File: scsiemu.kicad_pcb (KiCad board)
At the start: 2 copper layers, 65 x 41.7 mm, 38 parts, among them J1 RasPi, J2 SCSI, J3 USB_POWER, J4 POWER 5V, J5 I2C, U1 74LS641-1, U2 74LS641-1, U3 74LS641-1, U4 74LS641-1

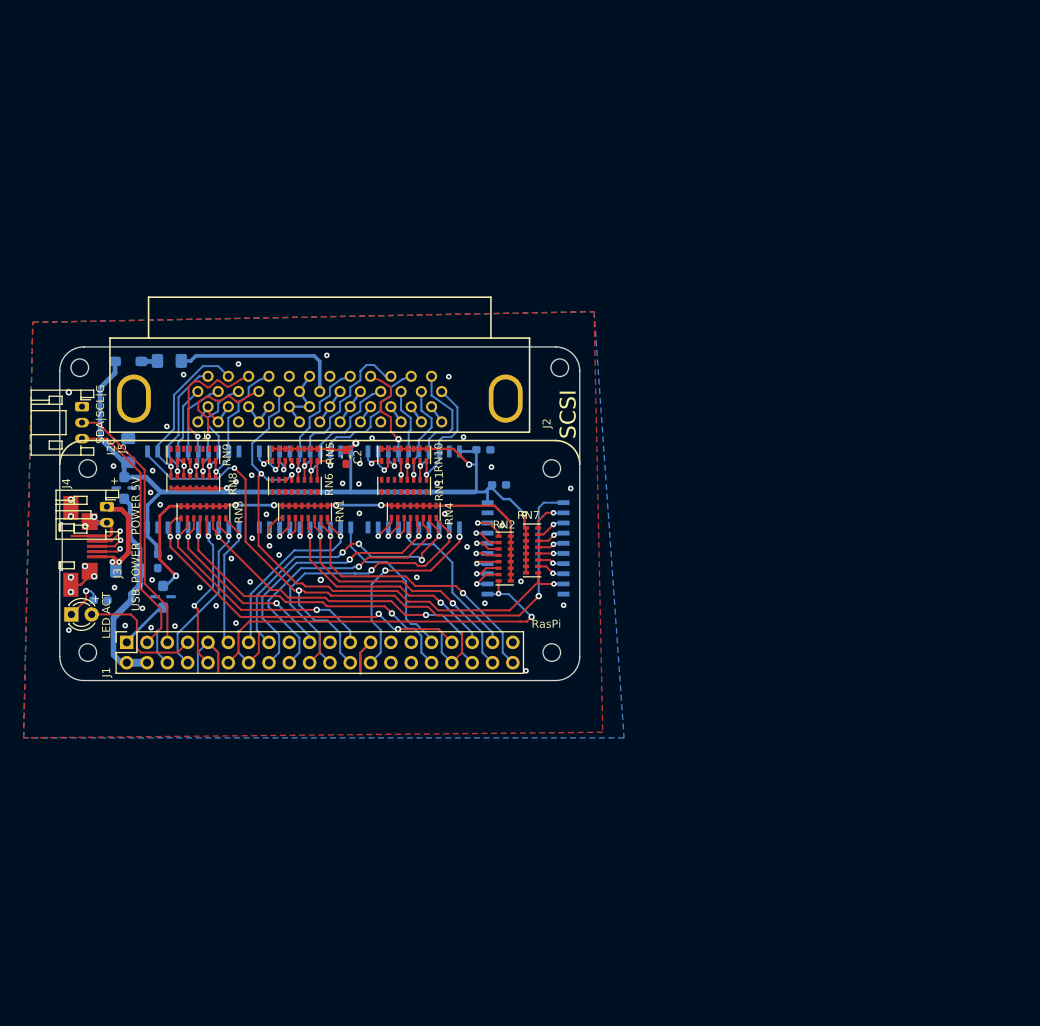
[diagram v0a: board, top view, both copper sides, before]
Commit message: Internal 50pin version (#1)
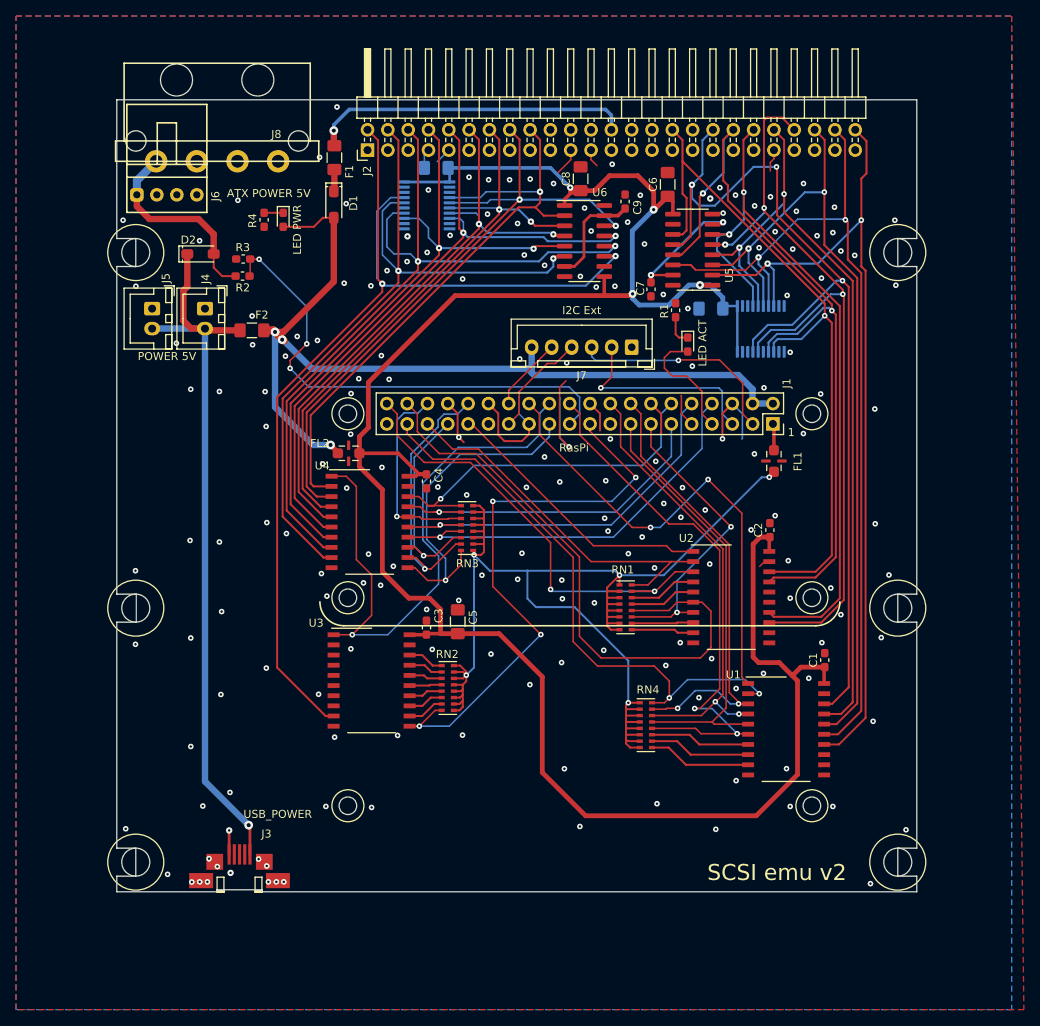
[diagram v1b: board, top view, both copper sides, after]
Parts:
- removed REF** (x6): MountingHole_2.2mm_M2, MountingHole:MountingHole_2.2mm_M2
- removed RN10, RN5, RN7, RN8: 220, Resistor_SMD:R_Cat16-8
- removed RN11, RN6, RN9: 330, Resistor_SMD:R_Cat16-8
- added C10: 10u, Capacitor_SMD:C_1206_3216Metric_Pad1.42x1.75mm_HandSolder, B.Cu at (183.9, 64.0)
- added C11: 10u, Capacitor_SMD:C_1206_3216Metric_Pad1.42x1.75mm_HandSolder, B.Cu at (149.6, 46.4)
- added C6: 10u, Capacitor_SMD:C_1206_3216Metric_Pad1.42x1.75mm_HandSolder, F.Cu at (178.5, 48.5)
- added C7: 2.2u, Capacitor_SMD:C_0603_1608Metric_Pad1.05x0.95mm_HandSolder, F.Cu at (176.4, 61.6)
- added C8: 10u, Capacitor_SMD:C_1206_3216Metric_Pad1.42x1.75mm_HandSolder, F.Cu at (167.6, 47.8)
- added C9: 2.2u, Capacitor_SMD:C_0603_1608Metric_Pad1.05x0.95mm_HandSolder, F.Cu at (173.2, 50.6)
- added D2: SBD, local_lib:D_SOD-123_HandSoldering, F.Cu at (120.1, 57.2)
- added J6: AT Power 5V (171826-4), local_lib:Molex_171826-4, F.Cu at (119.6, 49.8)
- added J7: I2C Ext, Connector_JST:JST_XH_B6B-XH-A_1x06_P2.50mm_Vertical, F.Cu at (174.0, 68.8)
- added J8: AT Power 5V (641737-1), local_lib:TE_641737-1, F.Cu at (122.2, 35.4)
- added LED2: LED ACT, LED_SMD:LED_0603_1608Metric_Pad1.05x0.95mm_HandSolder, F.Cu at (181.0, 68.5)
- added MH1: Raspi Mount, MountingHole:MountingHole_2.2mm_M2, F.Cu at (138.5, 100.2)
- added MH10: Raspi Mount, MountingHole:MountingHole_2.2mm_M2, F.Cu at (138.5, 126.2)
- added MH11: HDD Mount, MountingHole:MountingHole_3.5mm, F.Cu at (112.0, 101.5)
- added MH12: HDD Mount, MountingHole:MountingHole_3.5mm, F.Cu at (207.2, 101.5)
- added MH2: Raspi Mount, MountingHole:MountingHole_2.2mm_M2, F.Cu at (138.5, 77.2)
- added MH3: Raspi Mount, MountingHole:MountingHole_2.2mm_M2, F.Cu at (196.5, 77.2)
- added MH4: Raspi Mount, MountingHole:MountingHole_2.2mm_M2, F.Cu at (196.5, 100.2)
- added MH5: HDD Mount, MountingHole:MountingHole_3.5mm, F.Cu at (112.0, 57.0)
- added MH6: HDD Mount, MountingHole:MountingHole_3.5mm, F.Cu at (112.0, 133.2)
- added MH7: HDD Mount, MountingHole:MountingHole_3.5mm, F.Cu at (207.2, 57.0)
- added MH8: HDD Mount, MountingHole:MountingHole_3.5mm, F.Cu at (207.2, 133.2)
- added MH9: Raspi Mount, MountingHole:MountingHole_2.2mm_M2, F.Cu at (196.5, 126.2)
- added R2: 2.2k, Resistor_SMD:R_0603_1608Metric_Pad1.05x0.95mm_HandSolder, F.Cu at (125.3, 59.9)
- added R3: 2.7k, Resistor_SMD:R_0603_1608Metric_Pad1.05x0.95mm_HandSolder, F.Cu at (125.4, 57.8)
- added R4: 1k, Resistor_SMD:R_0603_1608Metric_Pad1.05x0.95mm_HandSolder, F.Cu at (128.0, 52.9)
- added U5: DS2105Z, Package_SO:SOIC-16_3.9x9.9mm_P1.27mm, F.Cu at (181.6, 56.6)
- added U6: DS2105Z, Package_SO:SOIC-16_3.9x9.9mm_P1.27mm, F.Cu at (168.1, 55.6)
- added U7: TL2218-285, Package_SO:TSSOP-20_4.4x6.5mm_P0.65mm, B.Cu at (190.1, 66.5)
- added U8: TL2218-285, Package_SO:TSSOP-20_4.4x6.5mm_P0.65mm, B.Cu at (148.4, 51.1)
- C1, C4: value 0.1u JB -> 0.1u; moved to F.Cu
- C2: value 0.1u JB -> 0.1u
- C3: value 0.1u JIS B -> 0.1u; moved to F.Cu
- C5: value 10u JB -> 10u; moved to F.Cu
- D1: footprint cd_device:D_SOD-123_HandSoldering -> local_lib:D_SOD-123_HandSoldering; moved to F.Cu
- F1: value 1A -> 750mA ~~ 1A (0ZCJ0075FF2E); moved to F.Cu
- F2: value 1A -> 2A (0685T2000-01); moved to F.Cu
- FL1, FL2, R1, U1, U2, U3, U4: moved to F.Cu
- J2: footprint local_lib:DSUB50P -> Connector_PinHeader_2.54mm:PinHeader_2x25_P2.54mm_Horizontal
- J4: footprint Connector_JST:JST_PH_S2B-PH-K_1x02_P2.00mm_Horizontal -> Connector_JST:JST_XH_B2B-XH-A_1x02_P2.50mm_Vertical
- J5: value I2C -> POWER 5V; footprint Connector_JST:JST_PH_S3B-PH-K_1x03_P2.00mm_Horizontal -> Connector_JST:JST_XH_B2B-XH-A_1x02_P2.50mm_Vertical
- LED1: value LED ACT -> LED PWR; footprint LED_THT:LED_D3.0mm -> LED_SMD:LED_0603_1608Metric_Pad1.05x0.95mm_HandSolder
- moved J1 85.3 mm to (191.6, 78.4), turned to 270 degrees
- moved R1 80.5 mm to (179.5, 64.2), turned to 90 degrees
- moved FL1 78.2 mm to (191.8, 83.1), turned to 270 degrees
- moved LED1 56.0 mm to (130.4, 52.9), turned to 270 degrees
- moved U1 55.4 mm to (193.3, 116.6), turned to 0 degrees
- moved U2 55.0 mm to (186.4, 100.1), turned to 0 degrees
- moved C2 53.7 mm to (191.3, 91.7), turned to 90 degrees
- moved C1 50.1 mm to (198.1, 108.0), turned to 90 degrees
- moved J3 46.8 mm to (125.0, 135.5), turned to 0 degrees
- moved C5 46.4 mm to (152.2, 103.1)
- moved RN1 41.8 mm to (173.2, 101.3), turned to 180 degrees
- moved RN4 39.4 mm to (175.8, 116.1), turned to 180 degrees
- moved C3 34.6 mm to (148.3, 103.9), turned to 90 degrees
- moved F2 33.8 mm to (126.5, 66.7)
- moved RN3 33.0 mm to (153.4, 91.4), turned to 0 degrees
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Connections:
- D1 pad 2: VCC -> /5V_DC
- F2 pad 1: Net-(F2-Pad1) -> /5V_DC
- F2 pad 2: Net-(F2-Pad2) -> Net-(D2-Pad1)
- FL2 pad 3: Net-(F2-Pad1) -> /5V_DC
- J1 pad 2: Net-(F2-Pad1) -> /5V_DC
- J1 pad 21: Net-(J1-Pad21) -> /AT_POWER_ON
- J1 pad 27: Net-(J1-Pad27) -> /EXT1
- J1 pad 28: Net-(J1-Pad28) -> /EXT2
- J1 pad 4: Net-(F2-Pad1) -> /5V_DC
- J2 pad 10: GND -> /S_D4
- J2 pad 12: GND -> /S_D5
- J2 pad 14: GND -> /S_D6
- J2 pad 16: GND -> /S_D7
- J2 pad 18: GND -> /S_DP
- J2 pad 2: GND -> /S_D0
- J2 pad 25: GND -> Net-(J2-Pad25)
- J2 pad 26: /S_D0 -> Net-(F1-Pad1)
- J2 pad 27: /S_D1 -> GND
- J2 pad 28: /S_D2 -> GND
- J2 pad 29: /S_D3 -> GND
- J2 pad 30: /S_D4 -> GND
- J2 pad 31: /S_D5 -> GND
- J2 pad 32: /S_D6 -> /S_ATN
- J2 pad 33: /S_D7 -> GND
- J2 pad 34: /S_DP -> Net-(J2-Pad34)
- J2 pad 36: GND -> /S_BSY
- J2 pad 38: Net-(F1-Pad1) -> /S_ACK
- J2 pad 4: GND -> /S_D1
- J2 pad 40: GND -> /S_RST
- J2 pad 41: Net-(J2-Pad41) -> GND
- J2 pad 42: GND -> /S_MSG
- J2 pad 43: Net-(J2-Pad43) -> GND
- J2 pad 44: Net-(J2-Pad44) -> /S_SEL
- J2 pad 45: Net-(J2-Pad45) -> GND
- J2 pad 46: Net-(J2-Pad46) -> /S_CD
- J2 pad 47: Net-(J2-Pad47) -> GND
- J2 pad 48: Net-(J2-Pad48) -> /S_REQ
- J2 pad 49: Net-(J2-Pad49) -> GND
- J2 pad 50: Net-(J2-Pad50) -> /S_IO
- J2 pad 6: GND -> /S_D2
- J2 pad 8: GND -> /S_D3
- J3 pad 1: Net-(F2-Pad2) -> Net-(D2-Pad1)
- J4 pad 1: Net-(F2-Pad2) -> GND
- J4 pad 2: GND -> Net-(D2-Pad1)
- J5 pad 2: /I2C_SCL -> Net-(D2-Pad1)
- LED1 pad 2: /ACT -> /5V_DC
- R1 pad 1: Net-(LED1-Pad1) -> Net-(LED2-Pad1)
- RN1 pad 3: Net-(RN1-Pad3) -> /SEL
- RN1 pad 4: Net-(RN1-Pad4) -> /RST
- RN1 pad 5: /ATN -> Net-(RN1-Pad5)
- RN1 pad 6: /RST -> Net-(RN1-Pad6)
- RN1 pad 8: /SEL -> /ATN
- RN2 pad 8: /DP -> /D0
- RN3 pad 1: /D3 -> /DP
- RN3 pad 2: /D1 -> /D7
- RN3 pad 3: /D0 -> /D6
- RN3 pad 4: /D2 -> /D5
- RN3 pad 5: /D5 -> /D4
- RN3 pad 6: /D6 -> /D3
- RN3 pad 7: /D4 -> /D2
- RN3 pad 8: /D7 -> /D1
- RN4 pad 4: /BSY -> /IO
- RN4 pad 5: /MSG -> /REQ
- RN4 pad 7: /REQ -> /MSG
- RN4 pad 8: /IO -> /BSY
- U1 pad 14: Net-(J2-Pad43) -> /S_IO
- U1 pad 15: Net-(J2-Pad46) -> /S_REQ
- U1 pad 16: Net-(J2-Pad48) -> /S_CD
- U1 pad 17: Net-(J2-Pad49) -> /S_MSG
- U1 pad 18: Net-(J2-Pad50) -> /S_BSY
- U1 pad 2: /IO -> /BSY
- U1 pad 3: /REQ -> /MSG
- U1 pad 5: /MSG -> /REQ
- U1 pad 6: /BSY -> /IO
- U2 pad 13: Net-(RN5-Pad3) -> /S_SEL
- U2 pad 14: Net-(RN5-Pad4) -> /S_RST
- U2 pad 15: Net-(J2-Pad41) -> Net-(U2-Pad15)
- U2 pad 16: Net-(J2-Pad45) -> Net-(U2-Pad16)
- U2 pad 17: Net-(J2-Pad44) -> /S_ACK
- U2 pad 18: Net-(J2-Pad47) -> /S_ATN
- U2 pad 2: /SEL -> /ATN
- U2 pad 4: /RST -> Net-(RN1-Pad6)
- U2 pad 5: /ATN -> Net-(RN1-Pad5)
- U2 pad 6: Net-(RN1-Pad4) -> /RST
- U2 pad 7: Net-(RN1-Pad3) -> /SEL
- U3 pad 11: /DP -> /D0
- U3 pad 9: /S_DP -> /S_D0
- U4 pad 11: /D7 -> /D1
- U4 pad 12: /D4 -> /D2
- U4 pad 13: /D6 -> /D3
- U4 pad 14: /D5 -> /D4
- U4 pad 15: /D2 -> /D5
- U4 pad 16: /D0 -> /D6
- U4 pad 17: /D1 -> /D7
- U4 pad 18: /D3 -> /DP
- U4 pad 2: /S_D3 -> /S_DP
- U4 pad 3: /S_D1 -> /S_D7
- U4 pad 4: /S_D0 -> /S_D6
- U4 pad 5: /S_D2 -> /S_D5
- U4 pad 6: /S_D5 -> /S_D4
- U4 pad 7: /S_D6 -> /S_D3
- U4 pad 8: /S_D4 -> /S_D2
- U4 pad 9: /S_D7 -> /S_D1
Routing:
- net VCC: track 132.8 -> 283.8 mm
- net /S_BSY: track 0.00 -> 120.2 mm, vias 0 -> 3
- net /5V_DC: track 0.00 -> 118.7 mm, vias 0 -> 3
- net /S_D0: track 12.7 -> 128.6 mm, vias 1 -> 2
- net /S_REQ: track 0.00 -> 111.0 mm, vias 0 -> 2
- net /S_IO: track 0.00 -> 108.2 mm, vias 0 -> 2
- net /S_CD: track 0.00 -> 104.9 mm, vias 0 -> 2
- net /S_SEL: track 0.00 -> 102.1 mm, vias 0 -> 3
- net /S_MSG: track 0.00 -> 100.8 mm, vias 0 -> 2
- net /S_ACK: track 0.00 -> 99.8 mm, vias 0 -> 2
- net /S_RST: track 0.00 -> 94.5 mm, vias 0 -> 2
- net VEE: track 63.2 -> 155.6 mm
- net Net-(D2-Pad1): track 0.00 -> 90.8 mm, vias 0 -> 1
- net /S_ATN: track 0.00 -> 89.8 mm, vias 0 -> 1
- net /S_D2: track 14.4 -> 99.8 mm, vias 1 -> 2
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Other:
- board size 65 x 41.7 mm -> 100 x 99 mm
- net class Default: clearance 0.2 -> 0.25; via_drill 0.4 -> 0.3
- net class LV added: clearance 0.2, trace_width 0.2, via_dia 0.7, via_drill 0.3
- rule trace_clearance: 0.2 -> 0.25
- board text added: "ATX POWER 5V"
- board text added: "SCSI emu v2"
- board text removed: "*"
- board text removed: "+"
- board text removed: "D+"
- board text removed: "D-"
- board text removed: "GND"
- board text removed: "ID"
- board text removed: "SCSI"
- board text removed: "SDA|SCL|G"
